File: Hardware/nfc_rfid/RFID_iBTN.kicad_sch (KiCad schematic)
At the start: 73 parts, among them J6 AFH34-S06FIA-1H, J7 BW0033AG-L3.4W0.9H1.8, J8 BW0033AG-L3.4W0.9H1.8, Q2 AO3400A, Q3 AO3401A, Q4 AO3400A, Q5 AO3400A, U1 LMV358AIDGKR, U2 LMV331IDCKR, U3 LMV358AIDGKR

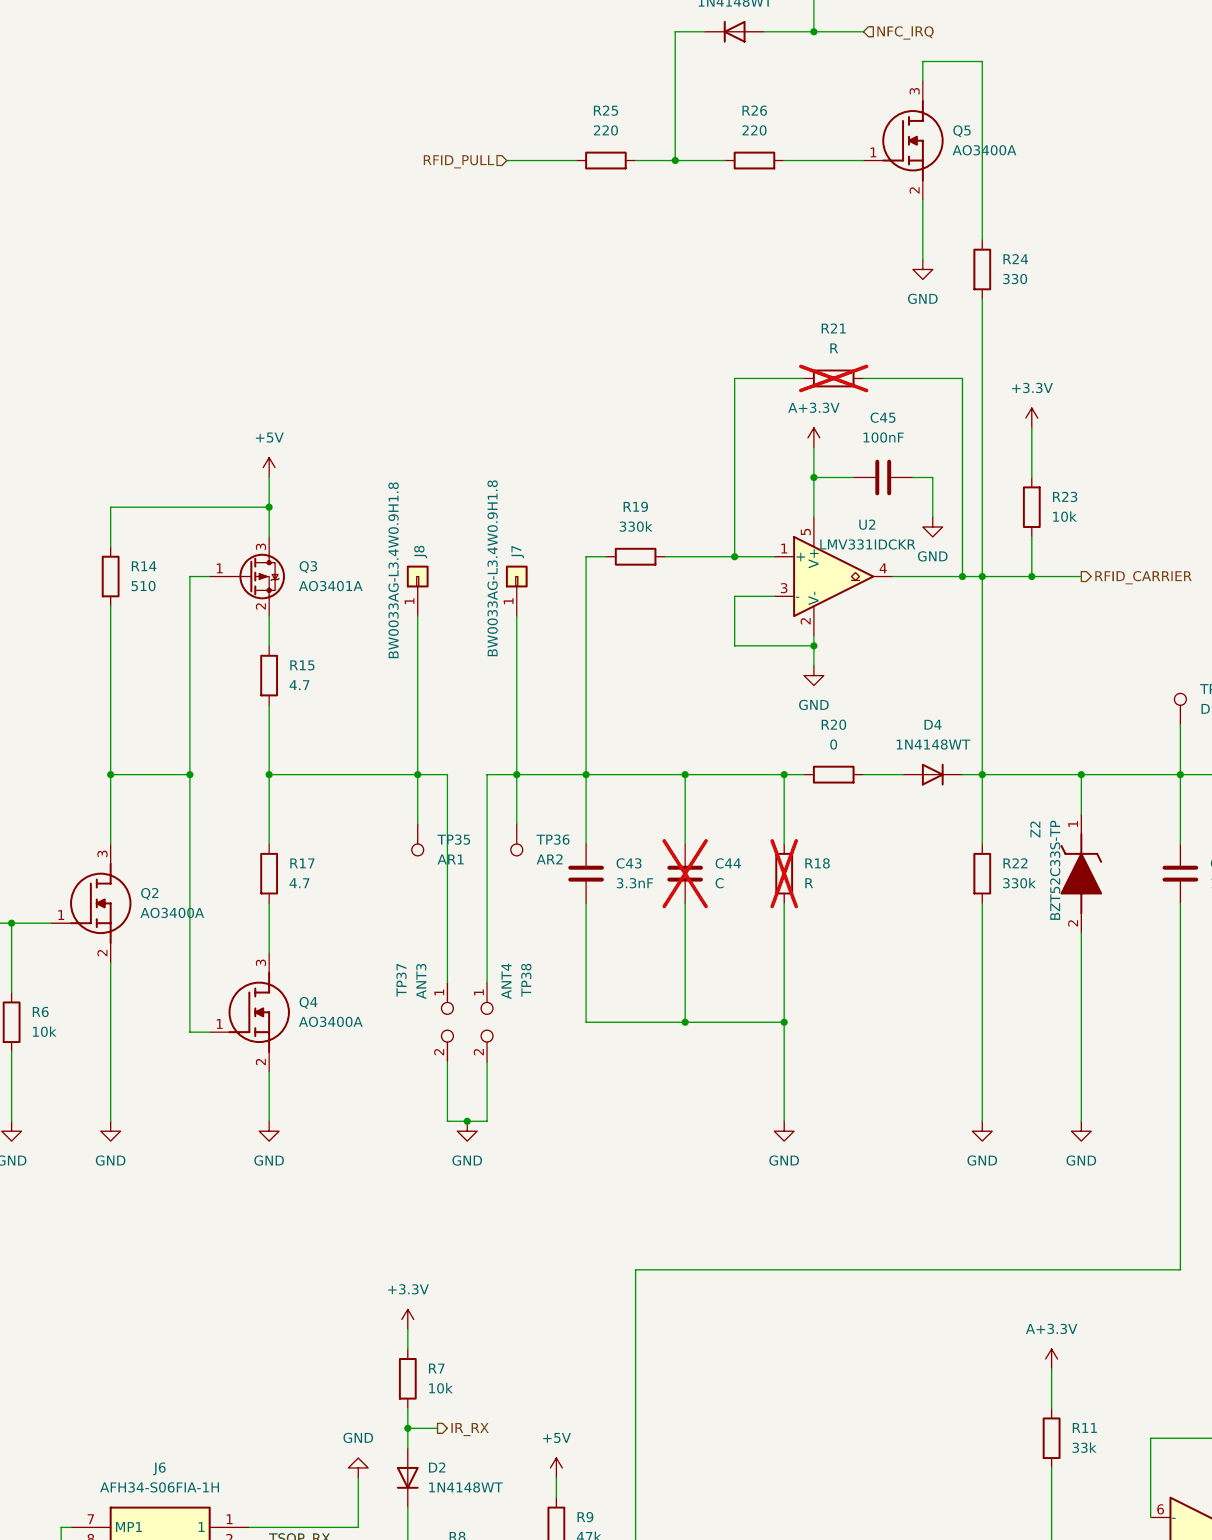
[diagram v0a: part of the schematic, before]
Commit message: PCB: Components placing done
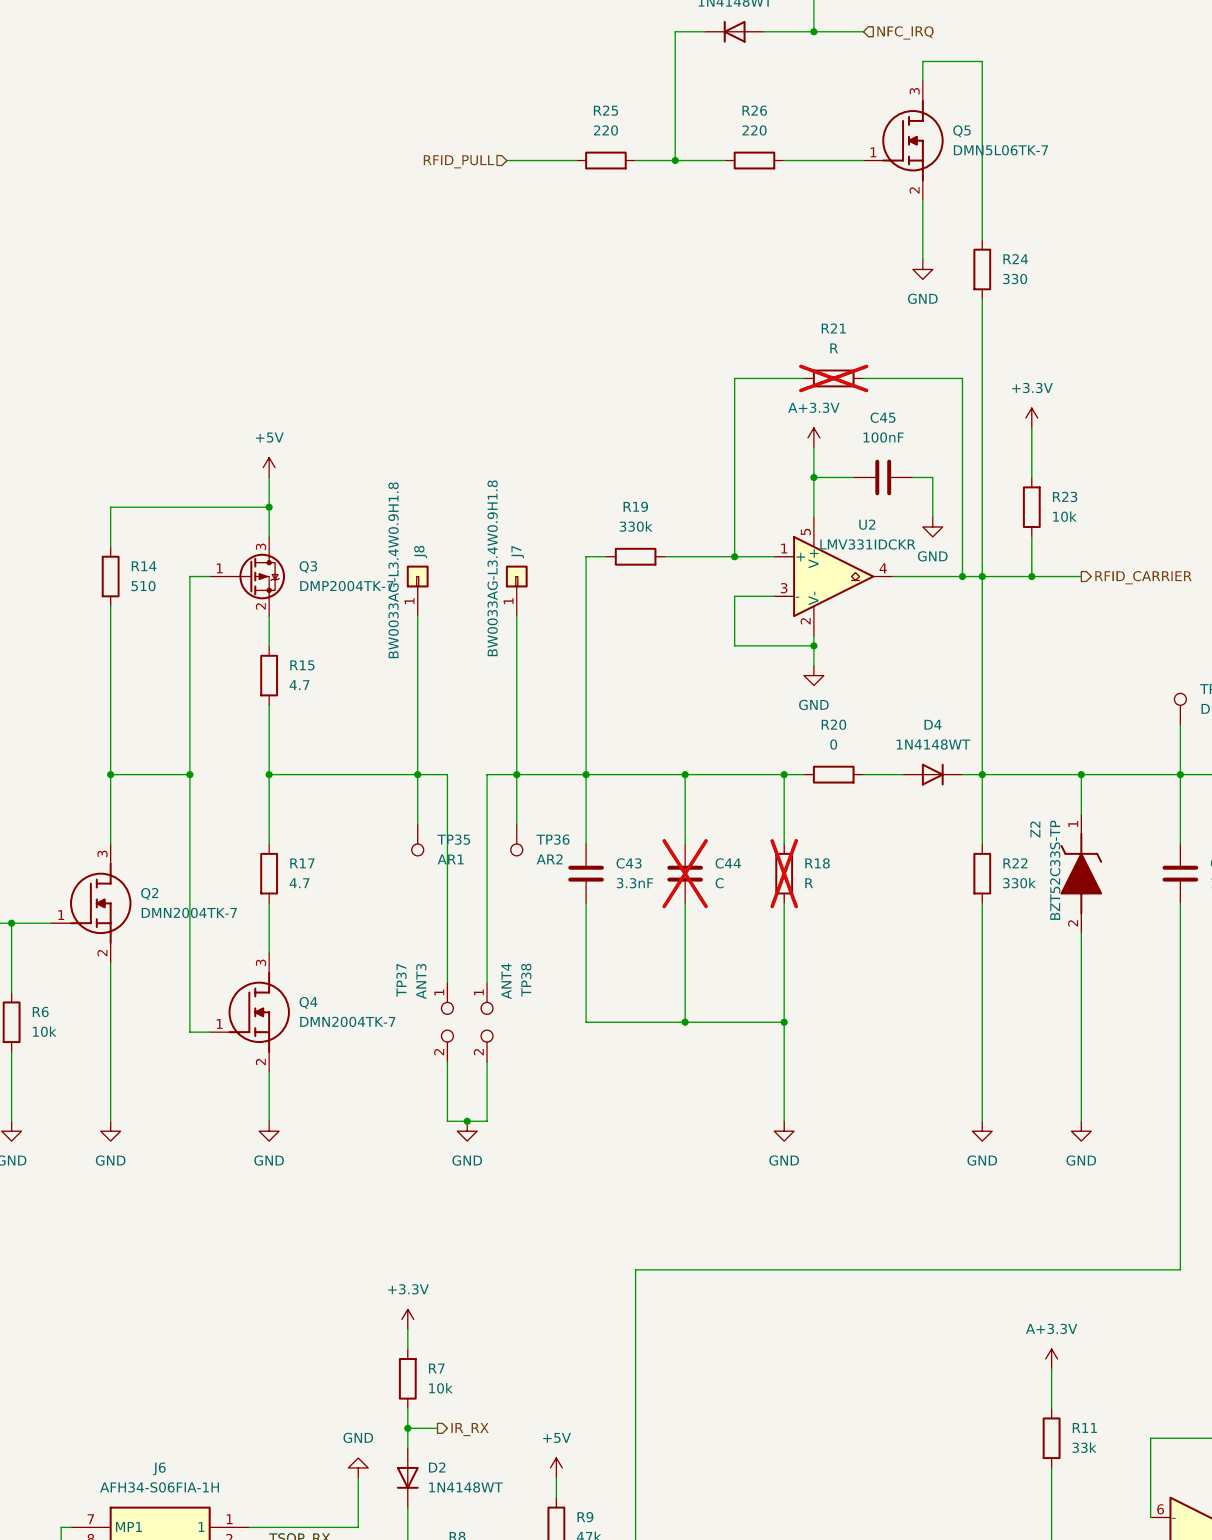
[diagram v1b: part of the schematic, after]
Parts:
- C39, C40, C41, C42, C45, C46, C47, C49, C50, C51, C52, C53, C54, C55: footprint (none) -> Capacitor_SMD:C_0402_1005Metric
- C43, C44: footprint (none) -> Capacitor_SMD:C_0805_2012Metric
- C48: footprint (none) -> Capacitor_SMD:C_1206_3216Metric
- J6: footprint AFH34S06FIA1H -> SamacSys_Parts:AFH34S06FIA1H
- Q2, Q4: value AO3400A -> DMN2004TK-7; footprint SOT95P280X125-3N -> Package_TO_SOT_SMD:SOT-523
- Q3: value AO3401A -> DMP2004TK-7; footprint Package_TO_SOT_SMD:SOT-23 -> Package_TO_SOT_SMD:SOT-523
- Q5: value AO3400A -> DMN5L06TK-7; footprint SOT95P280X125-3N -> Package_TO_SOT_SMD:SOT-523
- R10, R11, R12, R13, R14, R15, R17, R18, R19, R20, R21, R22, R23, R24, R25, R26, R27, R28, R29, R30, R31, R32, R33, R34, R35, R36, R37, R38, R6, R7, R8, R9: footprint (none) -> Resistor_SMD:R_0402_1005Metric
- TP33, TP34, TP35, TP36, TP39, TP40: footprint (none) -> TestPoint:TestPoint_Pad_1.0x1.0mm
- U1, U3: footprint (none) -> SamacSys_Parts:SOP65P490X110-8N
- U2: footprint (none) -> SamacSys_Parts:SOT65P210X110-5N
- Z2: footprint SOD2512X115N -> SamacSys_Parts:SOD2512X115N
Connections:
- net +3.3V: now also R7.2; no longer R7.1
- net IR_RX: now also R7.1; no longer R7.2
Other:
- moved on the sheet: R7

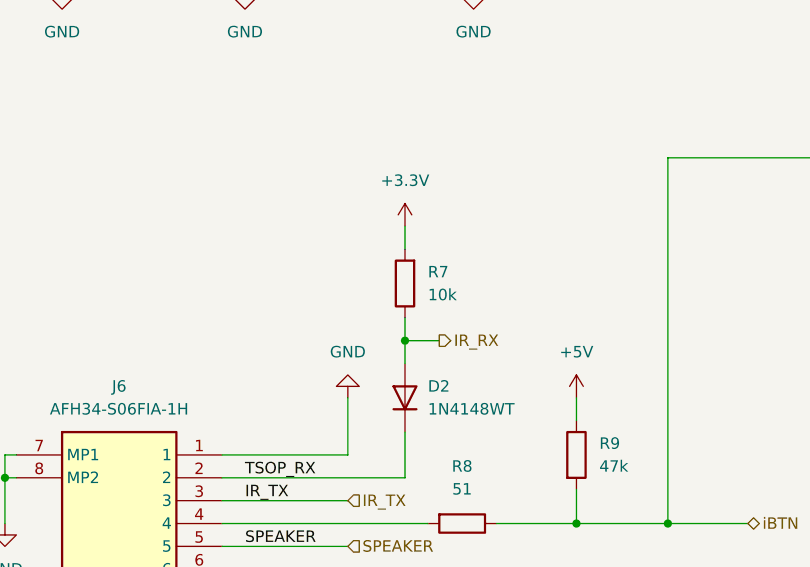
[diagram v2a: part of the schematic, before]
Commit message: PCB: add "remove from bom" entity; adjust design rule
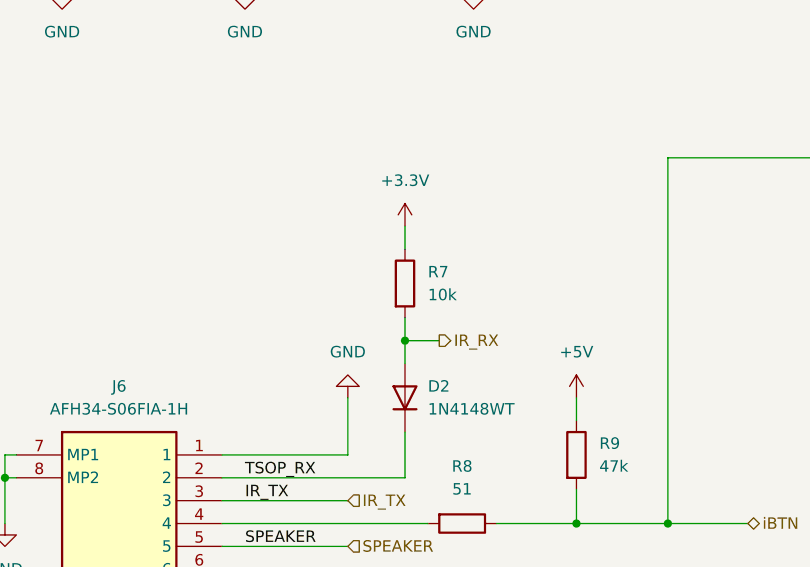
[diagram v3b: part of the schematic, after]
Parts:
- TP33, TP34, TP35, TP36, TP37, TP38, TP39, TP40: now left out of the parts list
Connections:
- net +3.3V: now also R7.1; no longer R7.2
- net IR_RX: now also R7.2; no longer R7.1
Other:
- moved on the sheet: R7
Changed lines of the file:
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@@
 	(symbol
 		(lib_id "Device:R")
-		(at 95.25 207.01 180)
+		(at 95.25 207.01 0)
 		(unit 1)
 		(exclude_from_sim no)
@@
 					(size 1.27 1.27)
 				)
-				(justify right)
+				(justify left)
 			)
 		)
@@
 					(size 1.27 1.27)
 				)
-				(justify right)
+				(justify left)
 			)
 		)
 		(property "Footprint" "Resistor_SMD:R_0402_1005Metric"
-			(at 97.028 207.01 90)
+			(at 93.472 207.01 90)
 			(effects
 				(font
@@
 		(unit 1)
 		(exclude_from_sim no)
-		(in_bom yes)
+		(in_bom no)
 		(on_board yes)
 		(dnp no)
@@
 		(unit 1)
 		(exclude_from_sim no)
-		(in_bom yes)
+		(in_bom no)
 		(on_board yes)
 		(dnp no)
@@
 		(unit 1)
 		(exclude_from_sim no)
-		(in_bom yes)
+		(in_bom no)
 		(on_board yes)
 		(dnp no)
@@
 		(unit 1)
 		(exclude_from_sim no)
-		(in_bom yes)
+		(in_bom no)
 		(on_board yes)
 		(dnp no)
@@
 		(unit 1)
 		(exclude_from_sim no)
-		(in_bom yes)
+		(in_bom no)
 		(on_board yes)
 		(dnp no)
@@
 		(unit 1)
 		(exclude_from_sim no)
-		(in_bom yes)
+		(in_bom no)
 		(on_board yes)
 		(dnp no)
@@
 		(unit 1)
 		(exclude_from_sim no)
-		(in_bom yes)
+		(in_bom no)
 		(on_board yes)
 		(dnp no)
@@
 		(unit 1)
 		(exclude_from_sim no)
-		(in_bom yes)
+		(in_bom no)
 		(on_board yes)
 		(dnp no)
